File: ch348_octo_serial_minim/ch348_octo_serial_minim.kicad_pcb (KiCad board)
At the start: 2 copper layers, 88.9 x 40.9 mm, 58 parts, among them J1 USB_C_Receptacle_USB2.0, J10 JLCPCB_3.5MM_SOCKET_C18166, J11 Conn_01x04, J12 JLCPCB_3.5MM_SOCKET_C18166, J13 Conn_01x04, J14 JLCPCB_3.5MM_SOCKET_C18166, J15 Conn_01x04, J16 JLCPCB_3.5MM_SOCKET_C18166, J17 Conn_01x04, J18 JLCPCB_3.5MM_SOCKET_C18166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

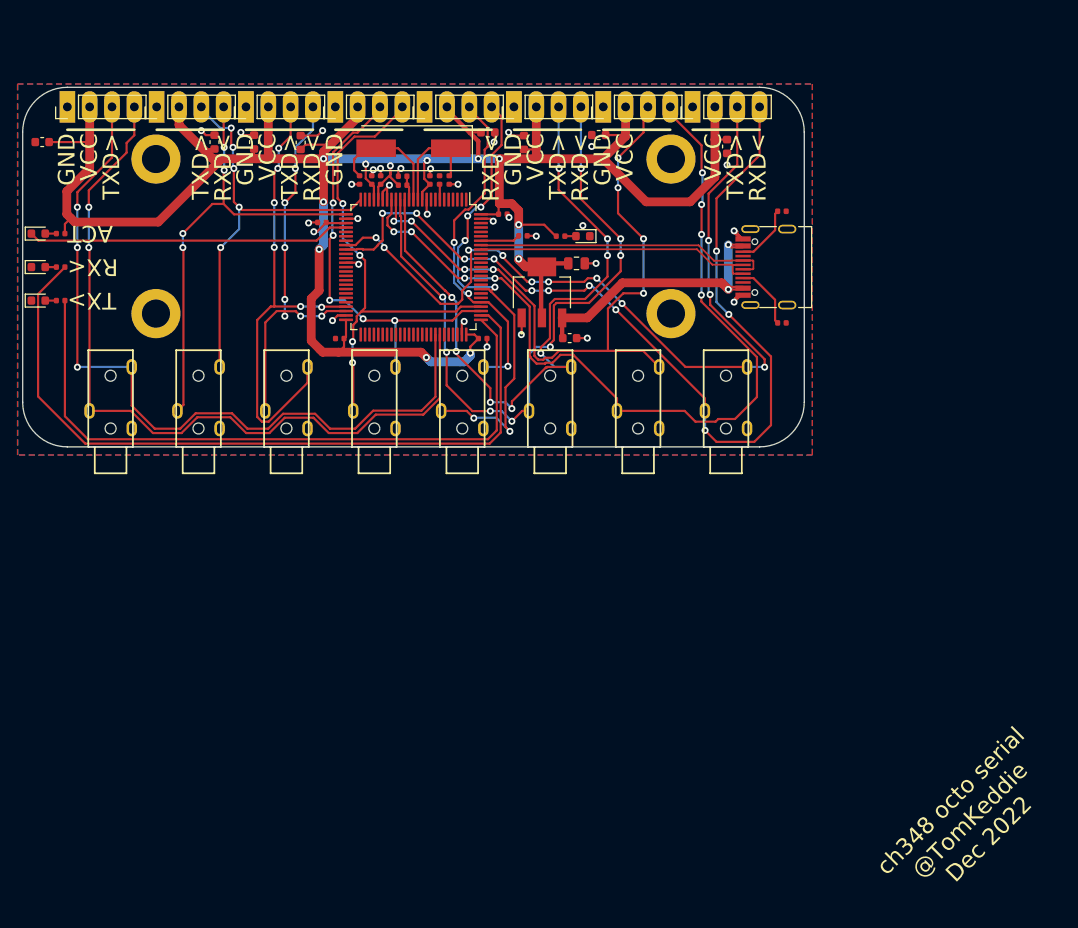
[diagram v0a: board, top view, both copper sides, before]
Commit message: ch348_octo_serial_minim: jan2023 rev ready for production
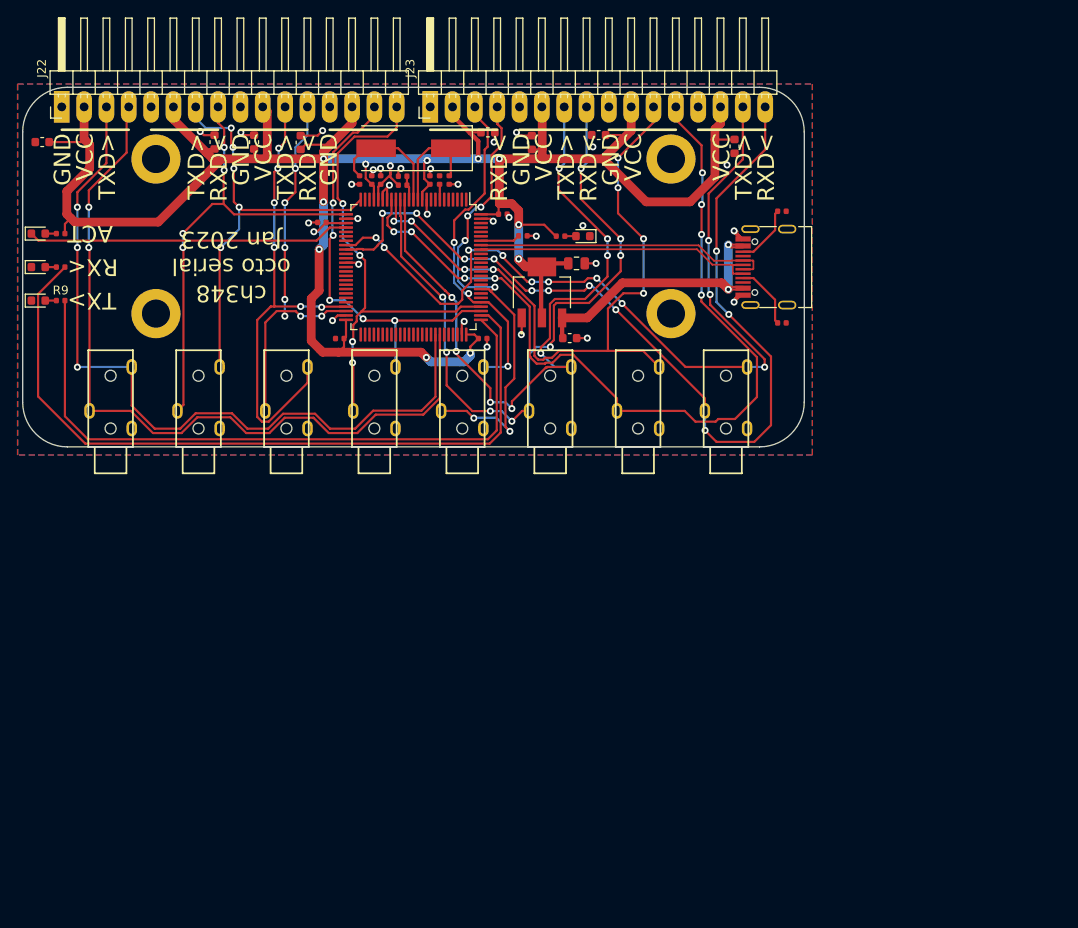
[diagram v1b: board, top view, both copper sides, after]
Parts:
- removed J11, J13, J15, J17, J19, J21, J7, J9: Conn_01x04, tom-connectors:PinHeader_1x04_P2.54mm_Vertical
- added J22: Conn_01x16, tom-connectors:PinHeader_1x16_P2.54mm_Horizontal, F.Cu at (73.0, 65.6)
- added J23: Conn_01x16, tom-connectors:PinHeader_1x16_P2.54mm_Horizontal, F.Cu at (114.9, 65.6)
- R1: value 1k -> 2.4k
- R9: value 1k -> 1.5k
- moved C14 0.90 mm to (126.5, 69.7)
- moved C16 0.85 mm to (149.6, 70.1)
- turned R9 to 0 degrees
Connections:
- R9 pad 1: /TX_S -> Net-(D4-Pad2)
- R9 pad 2: Net-(D4-Pad2) -> /TX_S
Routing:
- net +3.3V: track 265.4 -> 267.4 mm
- net /TXD6: track 76.4 -> 77.4 mm
- net /TXD3: track 48.3 -> 47.4 mm
- net /RXD3: track 54.5 -> 55.3 mm
- net /RXD0: track 89.5 -> 88.9 mm
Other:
- board text added: "ch348 octo serial Jan 2023"
- board text removed: "ch348 octo serial @TomKeddie Dec 2022"

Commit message: ch348_octo_serial_minim: move plate to subdir, add cts/rts link, Jan2023a
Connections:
- U1 pad 23: unconnected-(U1-Pad23) -> Net-(U1-Pad23)
- U1 pad 24: unconnected-(U1-Pad24) -> Net-(U1-Pad23)
- U1 pad 31: unconnected-(U1-Pad31) -> Net-(U1-Pad31)
- U1 pad 32: unconnected-(U1-Pad32) -> Net-(U1-Pad31)
- U1 pad 35: unconnected-(U1-Pad35) -> Net-(U1-Pad35)
- U1 pad 36: unconnected-(U1-Pad36) -> Net-(U1-Pad35)
- U1 pad 51: unconnected-(U1-Pad51) -> Net-(U1-Pad51)
- U1 pad 52: unconnected-(U1-Pad52) -> Net-(U1-Pad52)
- U1 pad 53: unconnected-(U1-Pad53) -> Net-(U1-Pad52)
- U1 pad 54: unconnected-(U1-Pad54) -> Net-(U1-Pad51)
- U1 pad 70: unconnected-(U1-Pad70) -> Net-(U1-Pad70)
- U1 pad 71: unconnected-(U1-Pad71) -> Net-(U1-Pad70)
- U1 pad 90: unconnected-(U1-Pad90) -> Net-(U1-Pad90)
- U1 pad 91: unconnected-(U1-Pad91) -> Net-(U1-Pad90)
- U1 pad 95: unconnected-(U1-Pad95) -> Net-(U1-Pad95)
- U1 pad 96: unconnected-(U1-Pad96) -> Net-(U1-Pad95)
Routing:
- net Net-(U1-Pad51): track 0.00 -> 3.67 mm
- net Net-(U1-Pad31): track 0.00 -> 2.73 mm
- net Net-(U1-Pad35): track 0.00 -> 2.68 mm
- net Net-(U1-Pad70): track 0.00 -> 2.63 mm
- net Net-(U1-Pad95): track 0.00 -> 2.63 mm
- net Net-(U1-Pad23): track 0.00 -> 2.58 mm
- net Net-(U1-Pad52): track 0.00 -> 2.53 mm
- net Net-(U1-Pad90): track 0.00 -> 0.50 mm
